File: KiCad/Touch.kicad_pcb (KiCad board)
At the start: 2 copper layers, 47.5 x 31 mm, 13 parts, among them P1 CONN_01X10, P2 CONN_01X05, P3 CONN_01X04, U1 MTCH6102_SSOP28

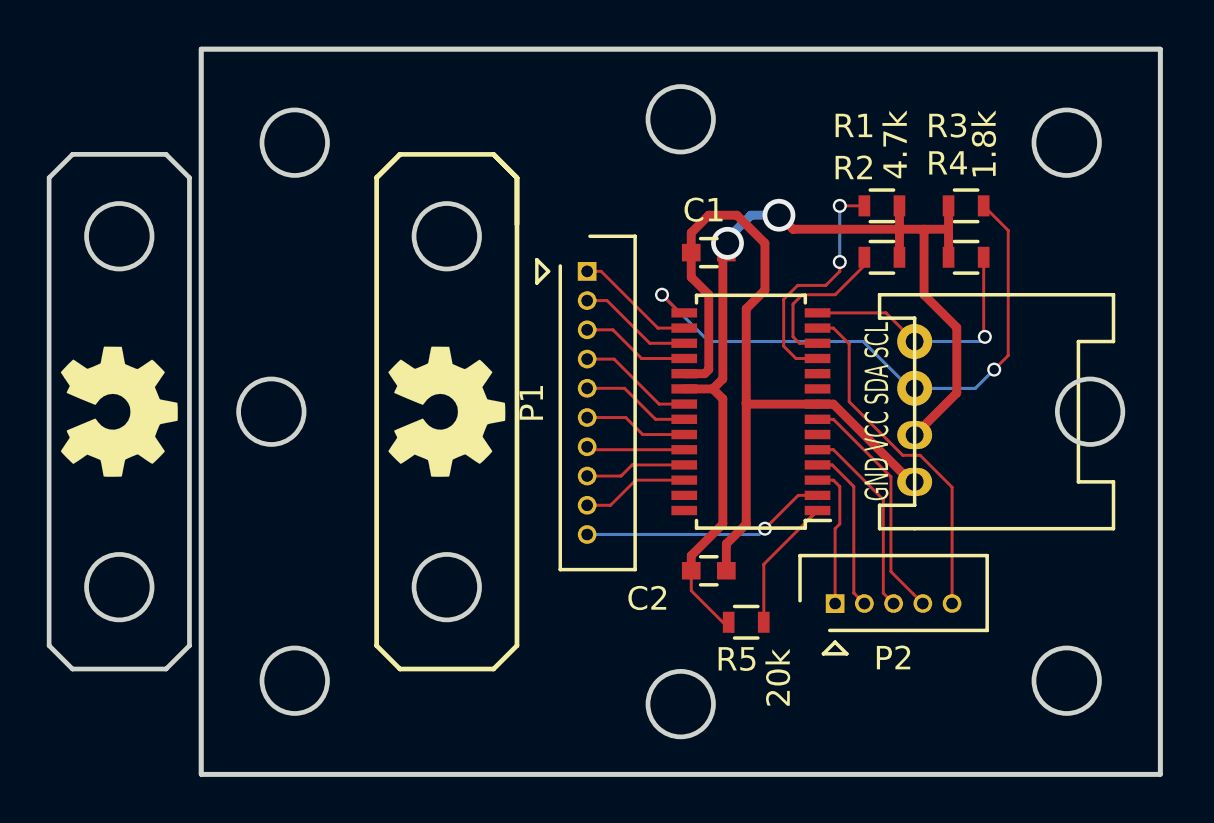
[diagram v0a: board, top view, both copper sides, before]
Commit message: add FPC connector.
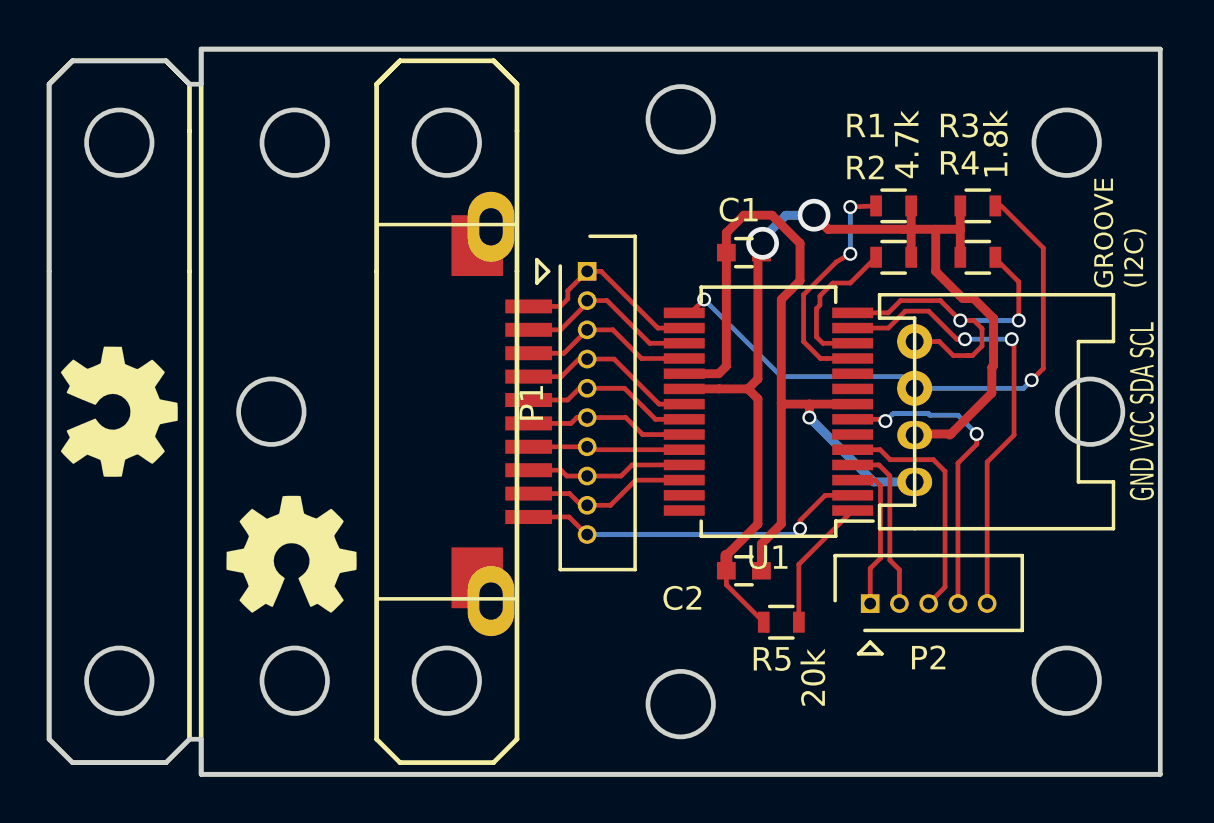
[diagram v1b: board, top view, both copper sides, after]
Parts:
- added P4: CONN_01X10, library:FFC_CONNECTOR_1.0D-WTS-10P, F.Cu at (96.1, 81.2)
- added REF**: 2x1_7.62mmScrewTerminal, library:2x1_7.62mmScrewTerminal, F.Cu at (98.1, 83.2)
- U1: footprint Housings_SSOP:TSSOP-28_4.4x9.7mm_Pitch0.65mm -> Housings_SSOP:SSOP-28_5.3x10.2mm_Pitch0.65mm
- moved OSHW 9.01 mm to (89.4, 87.3), turned to 0 degrees
- moved C1 1.50 mm to (108.8, 74.4)
- moved C2 1.50 mm to (108.8, 88.0)
- moved P2 1.50 mm to (114.2, 89.4)
- moved R5 1.50 mm to (110.4, 90.2)
- moved U1 0.75 mm to (109.8, 81.2)
- moved R1 0.50 mm to (115.2, 72.4)
- moved R2 0.50 mm to (115.2, 74.6)
- moved R3 0.50 mm to (118.8, 72.4)
- moved R4 0.50 mm to (118.8, 74.6)
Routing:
- net Net-(P1-Pad10): track 10.5 -> 16.0 mm
- net Net-(P2-Pad5): track 15.0 -> 20.1 mm, vias 0 -> 2
- net Net-(P3-Pad4): track 11.2 -> 15.9 mm, vias 1 -> 2
- net Net-(P2-Pad4): track 10.1 -> 14.2 mm, vias 0 -> 2
- net Net-(C1-Pad1): track 44.9 -> 48.3 mm
- net Net-(P1-Pad1): track 5.15 -> 8.48 mm
- net Net-(P1-Pad2): track 4.91 -> 7.99 mm
- net Net-(P2-Pad3): track 8.32 -> 11.4 mm
- net Net-(P1-Pad3): track 4.66 -> 7.58 mm
- net Net-(P1-Pad4): track 4.95 -> 7.76 mm
- net Net-(P1-Pad9): track 4.60 -> 7.30 mm
- net Net-(P1-Pad5): track 4.70 -> 7.41 mm
- net Net-(P1-Pad8): track 4.35 -> 6.95 mm
- net Net-(P1-Pad6): track 4.45 -> 7.05 mm
- net Net-(P1-Pad7): track 4.20 -> 6.70 mm
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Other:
- outline, holes or cut-outs redrawn
- board text added: "GND VCC SDA SDL"
- board text added: "GROOVE (I2C)"
